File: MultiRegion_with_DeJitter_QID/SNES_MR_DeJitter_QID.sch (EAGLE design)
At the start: 84 parts, among them J1 SNESCART_CONN_SPARSE_4, Q31 2SC2412, U1 SuperCIC_lock, U2 uIGR, U3 EPM7032AETC44-10N, U4 74HCT2G125DP, U5 CDCE913, U6 2G17TI_DBV, U7 TLV70033, U8 TLV70018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

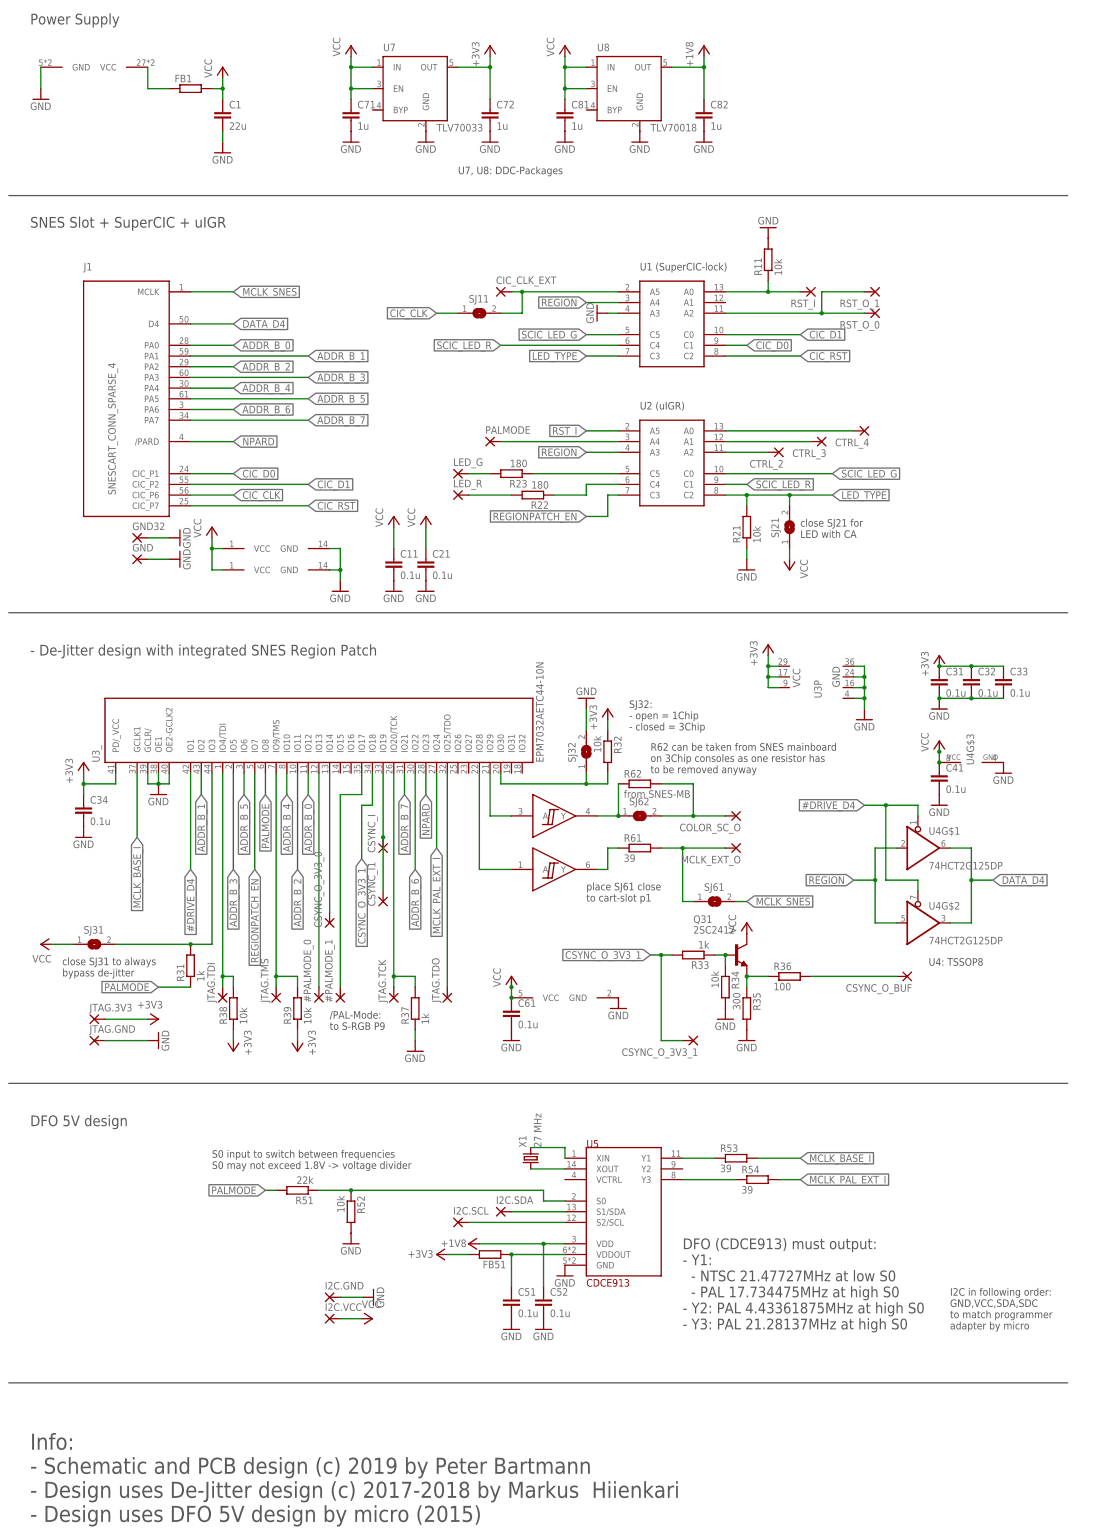
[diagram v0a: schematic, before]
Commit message: update PCB design: - selectable sync level for the buffered output - video buffer for sync instead of transistor
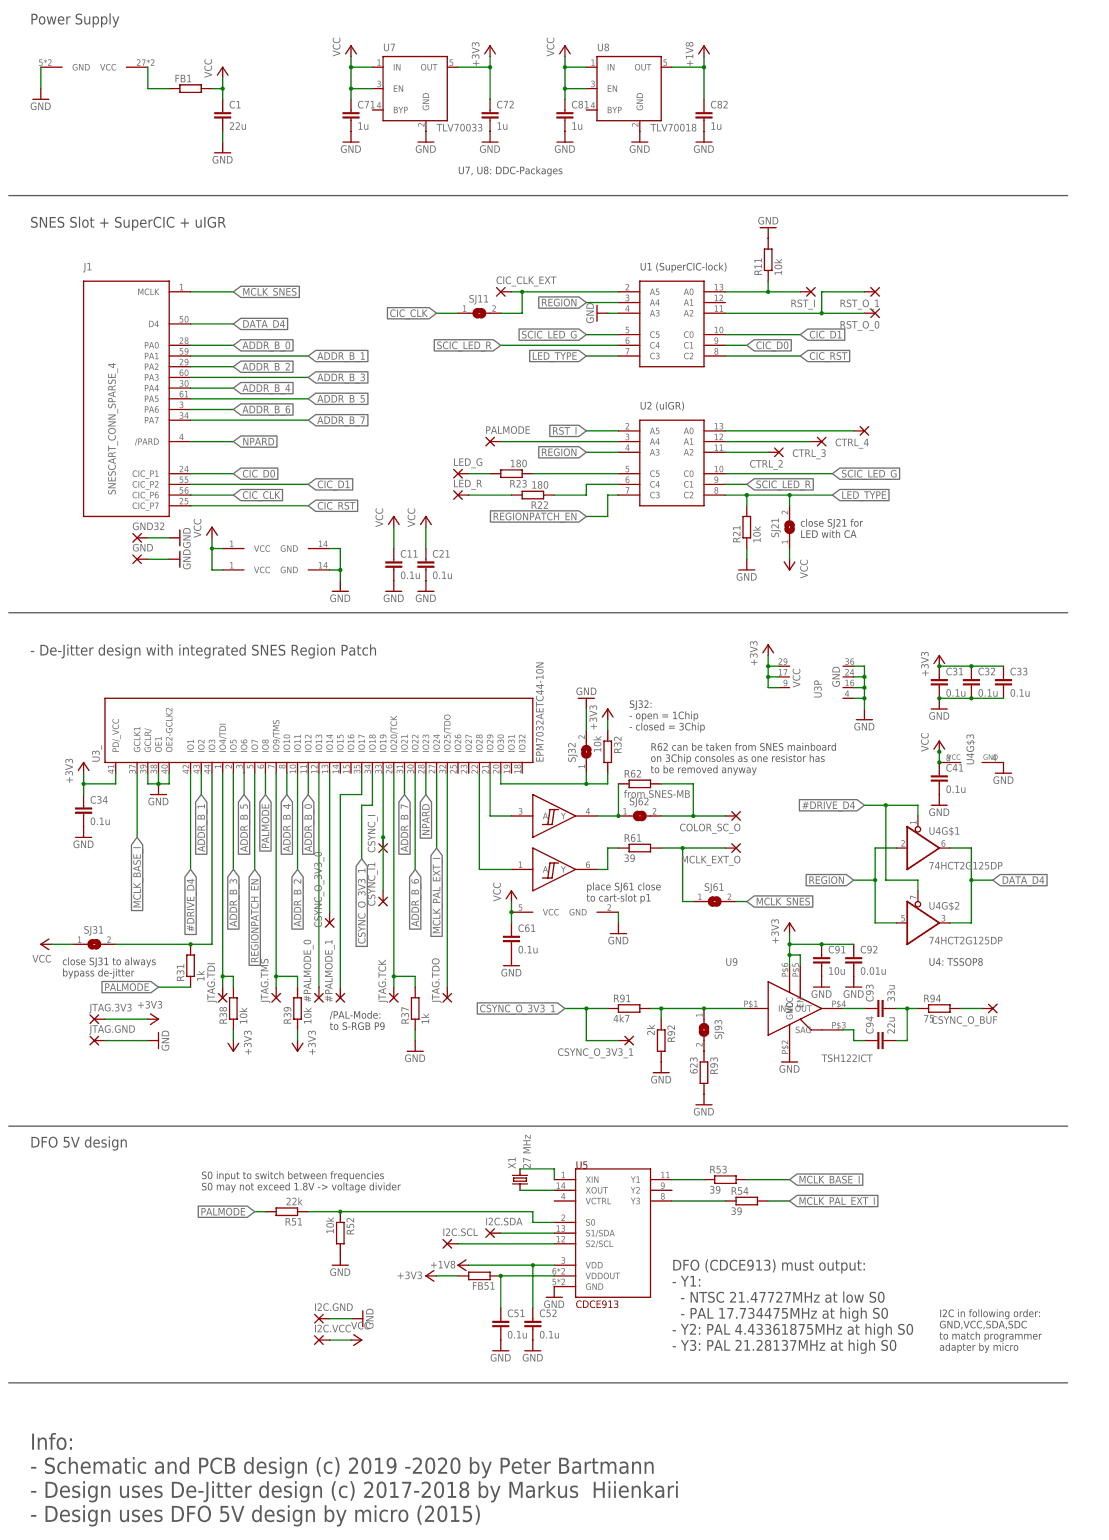
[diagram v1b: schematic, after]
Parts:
- removed Q31: 2SC2412, transistor:MMBTH24LT1-NPN-SOT23-BEC
- removed R33: 1k, rcl:R-EU_R0603
- removed R34: 10k, rcl:R-EU_R0603
- removed R35: 300, rcl:R-EU_R0603
- removed R36: 100, rcl:R-EU_R0603
- added C91: 10u, rcl:C-EUC0603
- added C92: 0.01u, rcl:C-EUC0603
- added C93: 33u, rcl:C-EUC0805
- added C94: 22u, rcl:C-EUC0603
- added R91: 4k7, rcl:R-EU_R0603
- added R92: 2k, rcl:R-EU_R0603
- added R93: 623, rcl:R-EU_R0603
- added R94: 75, rcl:R-EU_R0603
- added SJ93: (no value), jumper:SJSMALL
- added U9: TSH122ICT, st-microelectronics:TSH122ICT
- C1: device rcl:C-EUC0805 -> rcl:C-EUC0603
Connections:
- removed net CSYNC_O_POST_Q: Q31.E, R35.1, R36.1
- removed net CSYNC_O_PRE_Q: Q31.B, R33.1, R34.1
- new net N$1: R91.2, R92.1, SJ93.1, U9.IN
- new net N$10: R93.1, SJ93.2
- new net N$7: C94.1, U9.SAG
- new net N$8: C93.1, U9.OUT
- new net N$9: C93.2, C94.2, R94.1
- net +3V3: now also C91.1, C92.1, U9.EN, U9.VCC
- net +5V: no longer Q31.C
- net CSYNC_O: now also R94.2; no longer R36.2
- net CSYNC_O_3V3_1: now also R91.1; no longer R33.2
- net GND: now also C91.2, C92.2, R92.2, R93.2, U9.GND; no longer R34.2, R35.2
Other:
- note added: "Info: - Schematic and PCB design (c) 2019 -2020 by Peter Bartmann - Design uses De-Jitter design (c) 2017-2018 by Markus Hiienkari - Design uses DFO 5V design by micro (2015)"
- note removed: "Info: - Schematic and PCB design (c) 2019 by Peter Bartmann - Design uses De-Jitter design (c) 2017-2018 by Markus Hiienkari - Design uses DFO 5V design by micro (2015)"
- moved on the sheet: C51, C52, C61, CSYNC_O_3V3_1, CSYNC_O_BUF, FB51, I2C.GND, I2C.SCL, I2C.SDA, I2C.VCC, R51, R52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
